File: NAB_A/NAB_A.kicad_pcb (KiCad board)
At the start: 2 copper layers, 35 x 30 mm, 40 parts, among them K1 кнопка, K2 Кнопка_KLS7-TS5401-1.35-250-T, K2 кнопка, X1 Check_point

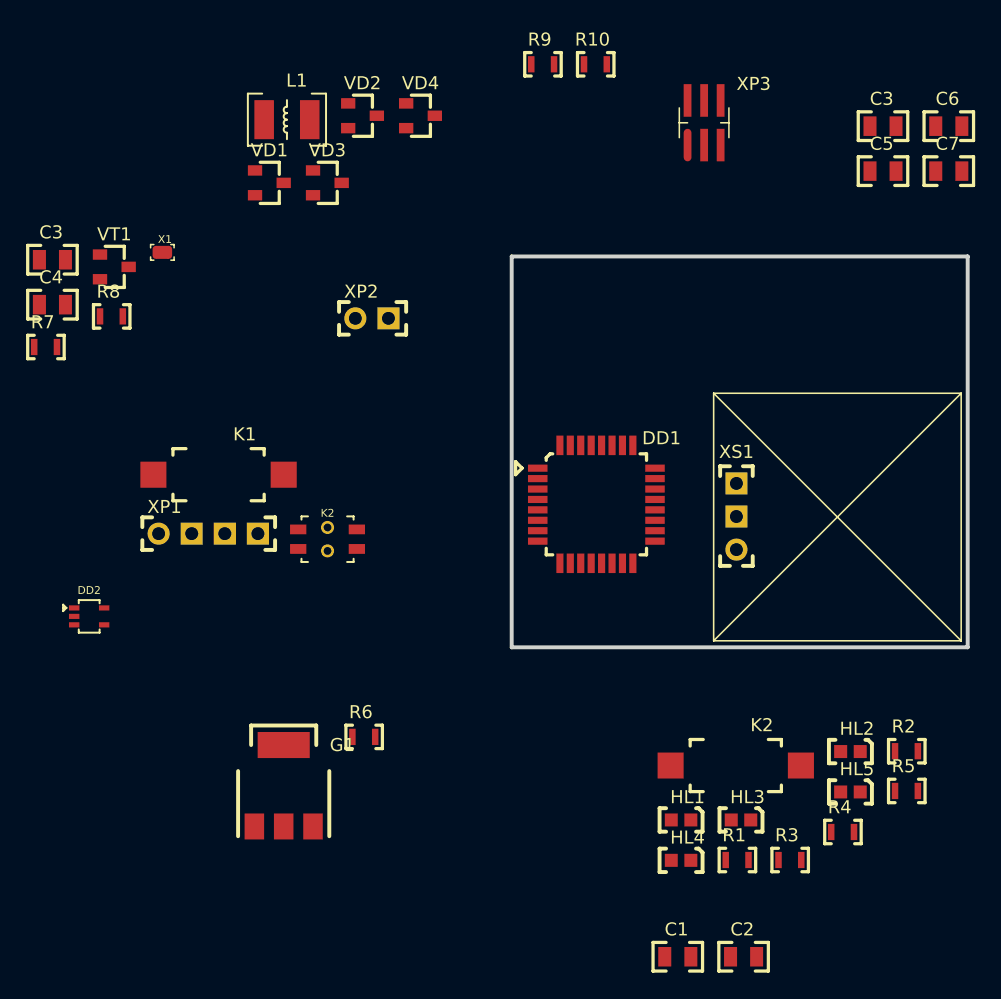
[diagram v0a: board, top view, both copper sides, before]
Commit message: NAB_A: готова трассировка, требуется проверка и дополнить трассировку
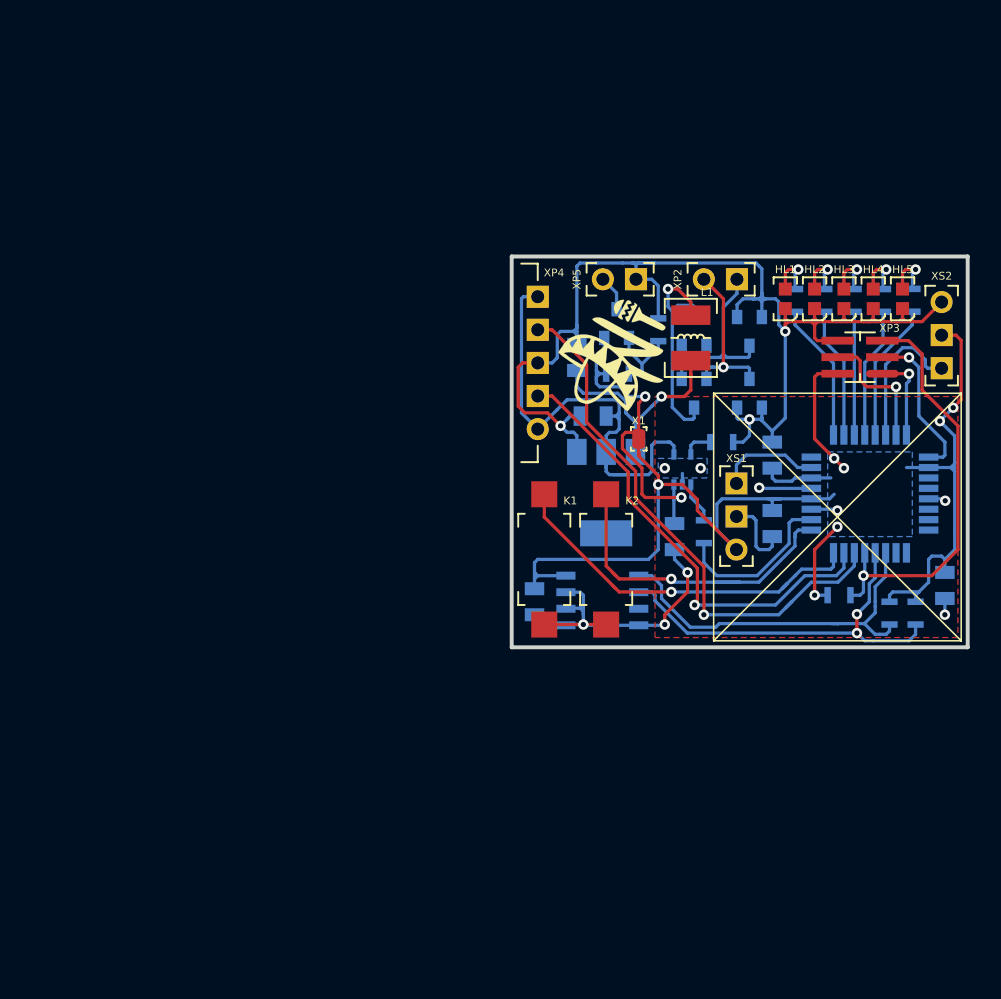
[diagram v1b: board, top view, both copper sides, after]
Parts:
- removed the C3 at (237.5, 30.0)
- removed the C3 at (173.8, 40.2)
- removed the K2 at (193.6, 62.5)
- removed R7, R8: Резистор_0,065Вт, N_RLC:Резистор_SMD_0603_0,065_Вт
- removed VT1: Транзистор_полевой_P-канал(IRLML2246TRPBF), N_VD_HL:Транзистор_IRLML6344TR_SOT-23
- removed XP1: Вилка_PLS4, N_X:Вилка_PLS4_вертикальная
- added BK1: Преобразователь_температуры_LM75AD, N_DD:SO-8, B.Cu at (217.0, 66.4)
- added C3: Конденсатор_керамический, N_RLC:Конденсатор_SMD_0805, B.Cu at (230.0, 56.2)
- added LOGO1: LOGO, N_ICO:ni_10x10, F.Cu at (218.2, 47.0)
- added R11: Резистор_0,065Вт, N_RLC:Резистор_SMD_0603_0,065_Вт, B.Cu at (239.0, 66.5)
- added R12: Резистор_0,065Вт, N_RLC:Резистор_SMD_0603_0,065_Вт, B.Cu at (241.0, 66.5)
- added R13: Резистор_0,065Вт, N_RLC:Резистор_SMD_0603_0,065_Вт, B.Cu at (221.2, 46.5)
- added R14: Резистор_0,065Вт, N_RLC:Резистор_SMD_0603_0,065_Вт, B.Cu at (217.2, 49.0)
- added VT2: Транзистор_полевой_P-канал(IRLML2246TRPBF), N_VD_HL:Транзистор_IRLML6344TR_SOT-23, B.Cu at (218.1, 45.1)
- added XP4: Вилка_PLS5, N_X:Вилка_угловая_XH.254_5, F.Cu at (212.0, 43.1)
- added XP5: Вилка_PLS2, N_X:Вилка_PLS2_вертикальная, F.Cu at (217.0, 41.8)
- added XS2: Розетка_PBS3, N_X:Розетка_PBS3_вертикальная, F.Cu at (243.0, 43.5)
- C1, C2, C4, C5, C6, C7, DD1, DD2, G1, R1, R10, R2, R3, R4, R5, R6, R9, VD1, VD2, VD3, VD4: moved to B.Cu
- moved R9 47.5 mm to (236.0, 66.0), turned to 180 degrees
- moved DD2 46.9 mm to (223.1, 56.4), turned to 90 degrees
- moved C2 46.5 mm to (215.0, 48.8), turned to 90 degrees
- moved HL4 46.5 mm to (237.8, 42.5), turned to 270 degrees
- moved C7 44.5 mm to (211.8, 65.5), turned to 270 degrees
- moved C4 44.3 mm to (217.2, 52.2), turned to 180 degrees
- moved R3 42.5 mm to (236.2, 44.2), turned to 90 degrees
- moved R1 42.4 mm to (231.8, 44.2), turned to 90 degrees
- moved HL1 41.7 mm to (231.0, 42.5), turned to 270 degrees
- moved HL3 41.7 mm to (235.5, 42.5), turned to 270 degrees
- moved VD1 40.2 mm to (228.2, 50.5), turned to 90 degrees
- moved R4 40.1 mm to (238.5, 44.2), turned to 90 degrees
- moved X1 39.3 mm to (219.8, 54.0), turned to 270 degrees
- moved HL5 38.9 mm to (240.0, 42.5), turned to 270 degrees
- moved R5 36.8 mm to (240.8, 44.2), turned to 90 degrees
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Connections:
- net Net-(L1-Pad1) renamed /QI+
- net Net-(VD1-Pad3) renamed /QI-1
- net Net-(VD2-Pad3) renamed /QI-2
- DD1 pad 1: Net-(DD1-Pad1) -> /BUT-2
- DD1 pad 10: Net-(DD1-Pad10) -> /HL-2
- DD1 pad 11: Net-(DD1-Pad11) -> /HL-3
- DD1 pad 12: Net-(DD1-Pad12) -> /HL-4
- DD1 pad 13: Net-(DD1-Pad13) -> /HL-5
- DD1 pad 14: Net-(DD1-Pad14) -> /DTH_DATA
- DD1 pad 15: Net-(DD1-Pad15) -> /MOSI
- DD1 pad 16: Net-(DD1-Pad16) -> /MISO
- DD1 pad 17: Net-(DD1-Pad17) -> /SCK
- DD1 pad 18: Net-(DD1-Pad18) -> /MC_VCC
- DD1 pad 2: Net-(DD1-Pad2) -> /CHARGE_STATUS
- DD1 pad 21: Net-(DD1-Pad21) -> /GND
- DD1 pad 27: Net-(DD1-Pad27) -> /SDA
- DD1 pad 28: Net-(DD1-Pad28) -> /SCL
- DD1 pad 29: Net-(DD1-Pad29) -> /nRESET
- DD1 pad 3: Net-(DD1-Pad3) -> /GND
- DD1 pad 30: Net-(DD1-Pad30) -> /MC_RX
- DD1 pad 31: Net-(DD1-Pad31) -> /MC_TX
- DD1 pad 32: Net-(DD1-Pad32) -> /BUT-1
- DD1 pad 4: Net-(DD1-Pad4) -> /MC_VCC
- DD1 pad 5: Net-(DD1-Pad5) -> /GND
- DD1 pad 6: Net-(DD1-Pad6) -> /MC_VCC
- DD1 pad 7: Net-(DD1-Pad7) -> /TX_DATA
- DD1 pad 9: Net-(DD1-Pad9) -> /HL-1
- K1 pad 1: Net-(K1-Pad1) -> /BUT-1
- K2 pad 1: Net-(K2-Pad1) -> /BUT-2
- R1 pad 1: Net-(R1-Pad1) -> /HL-1
- R2 pad 1: Net-(R2-Pad1) -> /HL-2
- R3 pad 1: Net-(R3-Pad1) -> /HL-3
- R4 pad 1: Net-(R4-Pad1) -> /HL-4
- R5 pad 1: Net-(R5-Pad1) -> /HL-5
- R9 pad 2: /5V -> /MC_VCC
- XP3 pad 2: /5V -> /MC_VCC
- XS1 pad 3: /DATA -> /TX_DATA
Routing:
- net /GND: track 0.00 -> 147.6 mm, vias 0 -> 12
- net /MC_VCC: track 0.00 -> 103.9 mm, vias 0 -> 7
- net /MC_RX: track 0.00 -> 42.6 mm, vias 0 -> 1
- net /5V: track 0.00 -> 37.3 mm
- net /MC_TX: track 0.00 -> 35.6 mm, vias 0 -> 1
- net /nRESET: track 0.00 -> 32.8 mm, vias 0 -> 1
- net /SCL: track 0.00 -> 30.7 mm, vias 0 -> 2
- net /BUT-1: track 0.00 -> 29.6 mm, vias 0 -> 1
- net /SDA: track 0.00 -> 29.1 mm
- net /BUT-2: track 0.00 -> 26.3 mm, vias 0 -> 1
- net /V_BAT: track 0.00 -> 25.7 mm, vias 0 -> 2
- net /: track 0.00 -> 20.4 mm, vias 0 -> 1
- net /QI+: track 0.00 -> 18.0 mm, vias 0 -> 1
- net /QI-1: track 0.00 -> 15.9 mm, vias 0 -> 1
- net /QI-2: track 0.00 -> 15.1 mm
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- added copper zone on B.Cu, net /GND
- added copper zone on F.Cu, net /GND
- added copper zone on B.Cu, net /MC_VCC
